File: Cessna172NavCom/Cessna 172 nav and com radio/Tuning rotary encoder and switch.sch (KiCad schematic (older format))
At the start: 7 parts, among them SW3 Tuning encoder

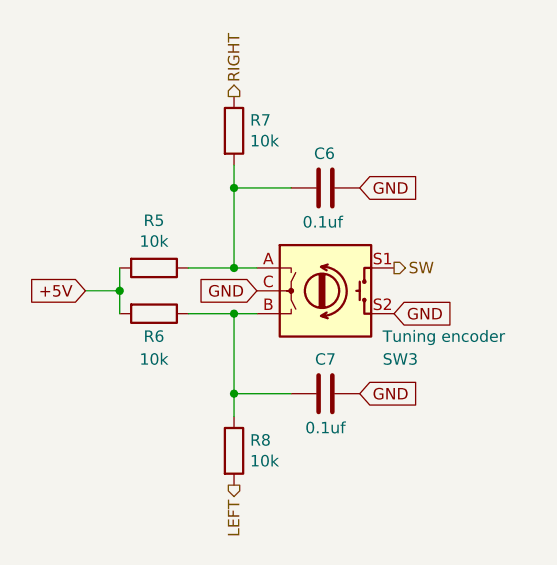
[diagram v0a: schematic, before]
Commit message: Tactile switch
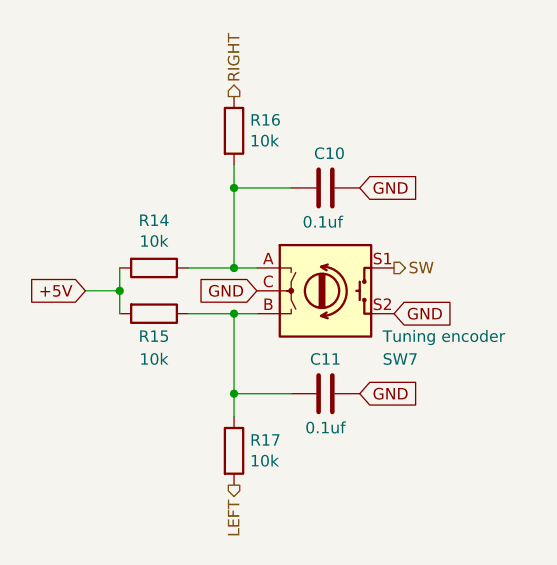
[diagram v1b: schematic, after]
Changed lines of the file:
@@
 $Descr A4 11693 8268
 encoding utf-8
-Sheet 5 8
+Sheet 7 8
 Title ""
 Date ""
@@
 AR Path="/5F5DD336/5F5D9322" Ref="SW4"  Part="1"
 AR Path="/5F5E0D77/5F5D9322" Ref="SW7"  Part="1"
-F 0 "SW3" H 6250 3650 50  0000 L CNN
+F 0 "SW7" H 6250 3650 50  0000 L CNN
 F 1 "Tuning encoder" H 6250 3750 50  0000 L CNN
 F 2 "Cessna 172 nav and com radio:EN11-HSM1BF20" H 5850 4110 50  0001 C CNN
@@
 AR Path="/5F5DD336/5F5D9328" Ref="R9"  Part="1"
 AR Path="/5F5E0D77/5F5D9328" Ref="R14"  Part="1"
-F 0 "R5" V 5043 3850 50  0000 C CNN
+F 0 "R14" V 5043 3850 50  0000 C CNN
 F 1 "10k" V 5134 3850 50  0000 C CNN
 F 2 "Resistor_SMD:R_0805_2012Metric_Pad1.15x1.40mm_HandSolder" V 5180 3850 50  0001 C CNN
@@
 AR Path="/5F5DD336/5F5D932E" Ref="R10"  Part="1"
 AR Path="/5F5E0D77/5F5D932E" Ref="R15"  Part="1"
-F 0 "R6" V 5350 4050 50  0000 C CNN
+F 0 "R15" V 5350 4050 50  0000 C CNN
 F 1 "10k" V 5450 4050 50  0000 C CNN
 F 2 "Resistor_SMD:R_0805_2012Metric_Pad1.15x1.40mm_HandSolder" V 5180 4050 50  0001 C CNN
@@
 AR Path="/5F5DD336/5F5D9337" Ref="C9"  Part="1"
 AR Path="/5F5E0D77/5F5D9337" Ref="C11"  Part="1"
-F 0 "C7" V 6150 4400 50  0000 C CNN
+F 0 "C11" V 6150 4400 50  0000 C CNN
 F 1 "0.1uf" V 5850 4400 50  0000 C CNN
 F 2 "Capacitor_SMD:C_0805_2012Metric_Pad1.15x1.40mm_HandSolder" H 6038 4250 50  0001 C CNN
@@
 AR Path="/5F5DD336/5F5D933D" Ref="C8"  Part="1"
 AR Path="/5F5E0D77/5F5D933D" Ref="C10"  Part="1"
-F 0 "C6" V 5850 3450 50  0000 L CNN
+F 0 "C10" V 5850 3450 50  0000 L CNN
 F 1 "0.1uf" V 6150 3400 50  0000 L CNN
 F 2 "Capacitor_SMD:C_0805_2012Metric_Pad1.15x1.40mm_HandSolder" H 6038 3350 50  0001 C CNN
@@
 AR Path="/5F5DD336/5F5D934C" Ref="R12"  Part="1"
 AR Path="/5F5E0D77/5F5D934C" Ref="R17"  Part="1"
-F 0 "R8" H 5670 4696 50  0000 L CNN
+F 0 "R17" H 5670 4696 50  0000 L CNN
 F 1 "10k" H 5670 4605 50  0000 L CNN
 F 2 "Resistor_SMD:R_0805_2012Metric_Pad1.15x1.40mm_HandSolder" V 5530 4650 50  0001 C CNN
@@
 AR Path="/5F5DD336/5F5D935D" Ref="R11"  Part="1"
 AR Path="/5F5E0D77/5F5D935D" Ref="R16"  Part="1"
-F 0 "R7" H 5670 3296 50  0000 L CNN
+F 0 "R16" H 5670 3296 50  0000 L CNN
 F 1 "10k" H 5670 3205 50  0000 L CNN
 F 2 "Resistor_SMD:R_0805_2012Metric_Pad1.15x1.40mm_HandSolder" V 5530 3250 50  0001 C CNN
